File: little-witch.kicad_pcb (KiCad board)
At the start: 4 copper layers, 65 x 30 mm, 56 parts, among them J1 GCT-USB4105, J2 TMJG0803HENL, J3 Conn_ARM_SWD_TagConnect_TC203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, J4 GCT-USB4105, J5 Conn_02x20_Odd_Even, J6 BOOT0_SEL, SW1 SW_Push, U1 CH32V307RCT6, U2 MXL86110C-AQB-R, Y1 SIT8008BI-73-33N-25.000000

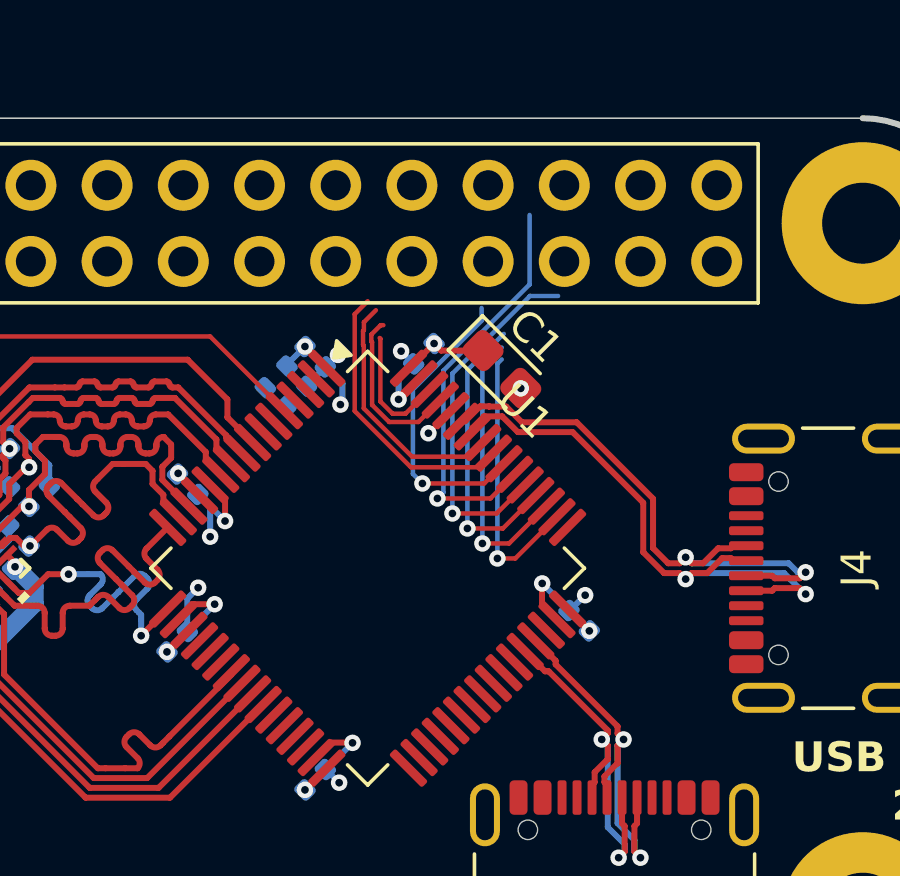
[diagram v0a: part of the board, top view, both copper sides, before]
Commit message: GPIO routing
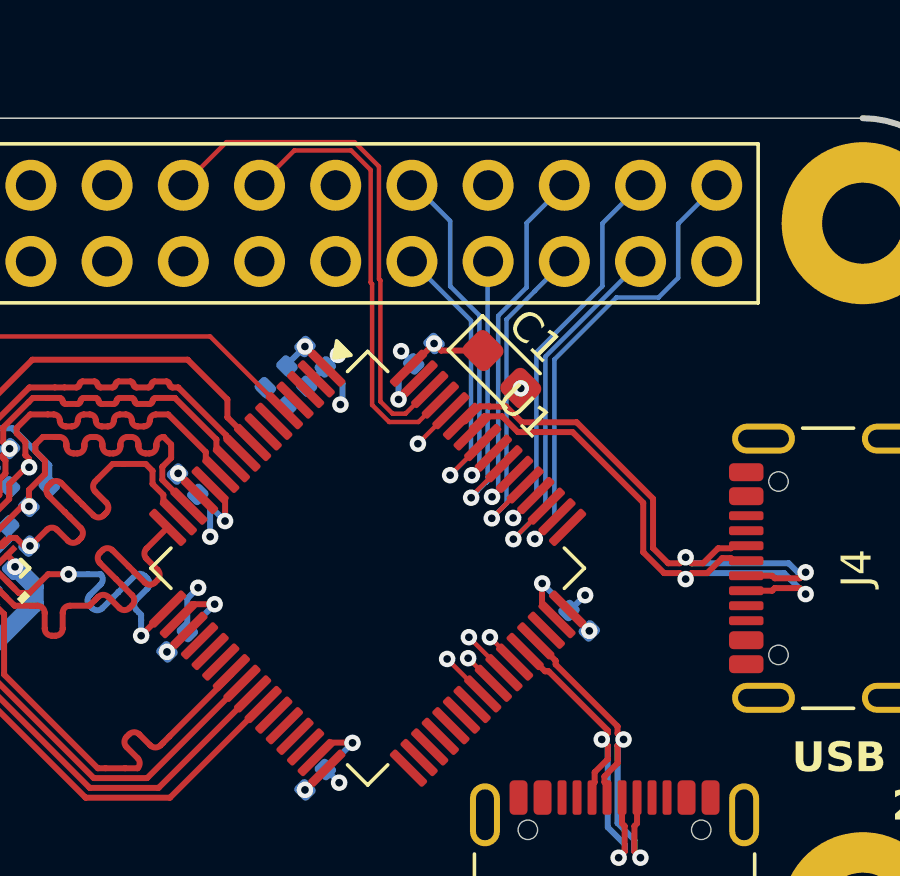
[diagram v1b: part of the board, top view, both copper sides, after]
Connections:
- J5 pad 26: unconnected-(J5-Pin_26-Pad26) -> /PB9
- J5 pad 28: unconnected-(J5-Pin_28-Pad28) -> /PB8
- J5 pad 31: unconnected-(J5-Pin_31-Pad31) -> /PB5
- J5 pad 32: unconnected-(J5-Pin_32-Pad32) -> /PB4
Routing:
- net /PB9: track 4.27 -> 17.5 mm
- net /PB8: track 5.70 -> 15.1 mm
- net /PA15: track 9.25 -> 16.2 mm
- net /PC11: track 9.72 -> 13.9 mm
- net /PC10: track 9.44 -> 12.6 mm
- net /PB4: track 9.43 -> 11.8 mm, vias 0 -> 1
- net /PC9: track 0.00 -> 1.67 mm, vias 0 -> 1
- net /PA9: track 0.00 -> 1.67 mm, vias 0 -> 1
- net /PB5: track 8.29 -> 9.77 mm, vias 0 -> 1
- net /PA8: track 0.00 -> 1.19 mm, vias 0 -> 1
- net /PD2: track 13.6 -> 12.4 mm
- net /PA10: track 0.00 -> 1.17 mm, vias 0 -> 1
- net /PC12: track 12.1 -> 11.1 mm

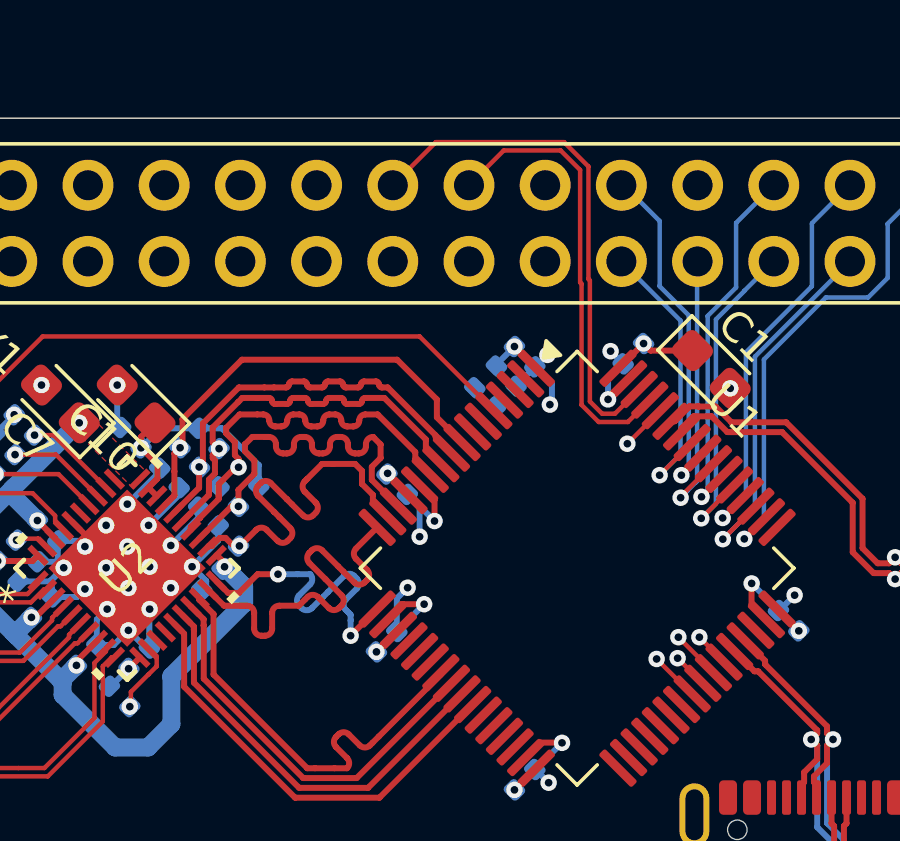
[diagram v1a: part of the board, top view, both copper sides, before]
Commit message: More GPIO routing
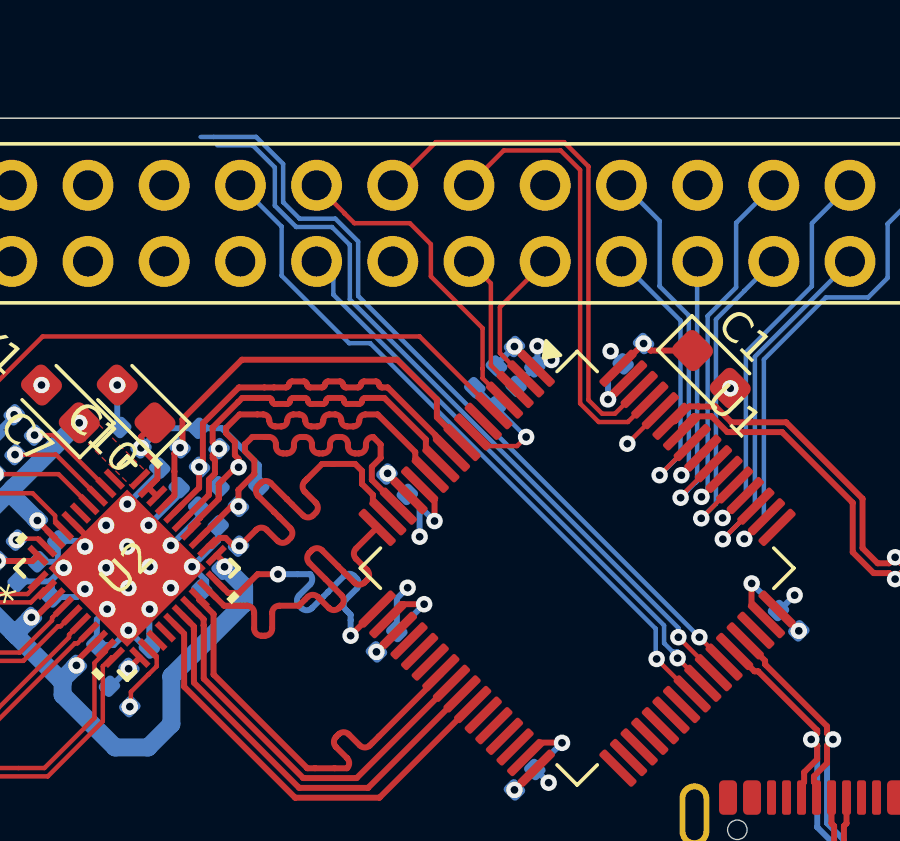
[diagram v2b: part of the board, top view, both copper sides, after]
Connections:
- J5 pad 22: unconnected-(J5-Pin_22-Pad22) -> /PC9
- J5 pad 23: unconnected-(J5-Pin_23-Pad23) -> /PA8
- J5 pad 24: unconnected-(J5-Pin_24-Pad24) -> /PC15
- J5 pad 27: unconnected-(J5-Pin_27-Pad27) -> /PC14
- J5 pad 29: unconnected-(J5-Pin_29-Pad29) -> /PC13
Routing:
- net /PA10: track 1.17 -> 26.5 mm
- net /PA9: track 1.67 -> 25.8 mm
- net /PC9: track 1.67 -> 23.6 mm
- net /PA8: track 1.19 -> 19.5 mm
- net /PC15: track 0.00 -> 10.8 mm
- net /PC13: track 0.00 -> 4.92 mm
- net /PC14: track 0.00 -> 4.90 mm
- net NRST: track 0.00 -> 4.49 mm, vias 0 -> 1
- net GND: track 42.7 -> 42.0 mm

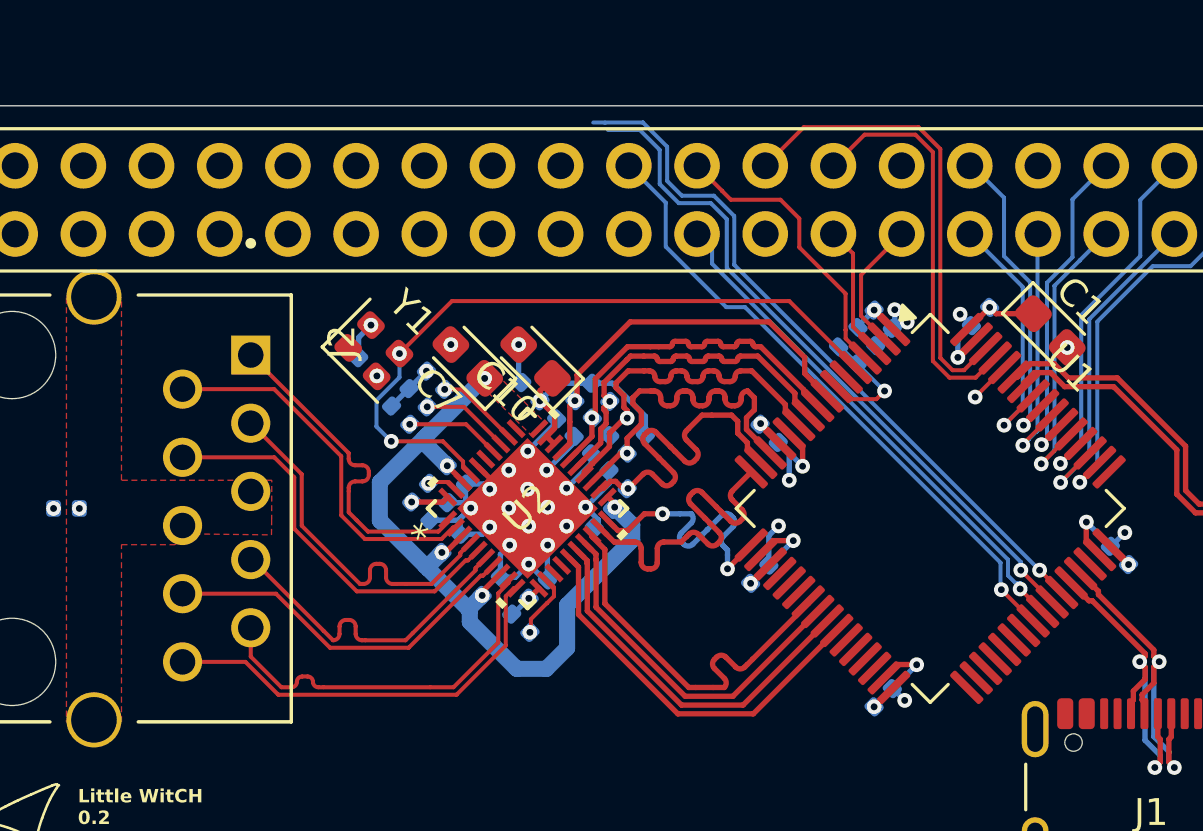
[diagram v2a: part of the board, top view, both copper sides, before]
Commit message: Yet more GPIO routing
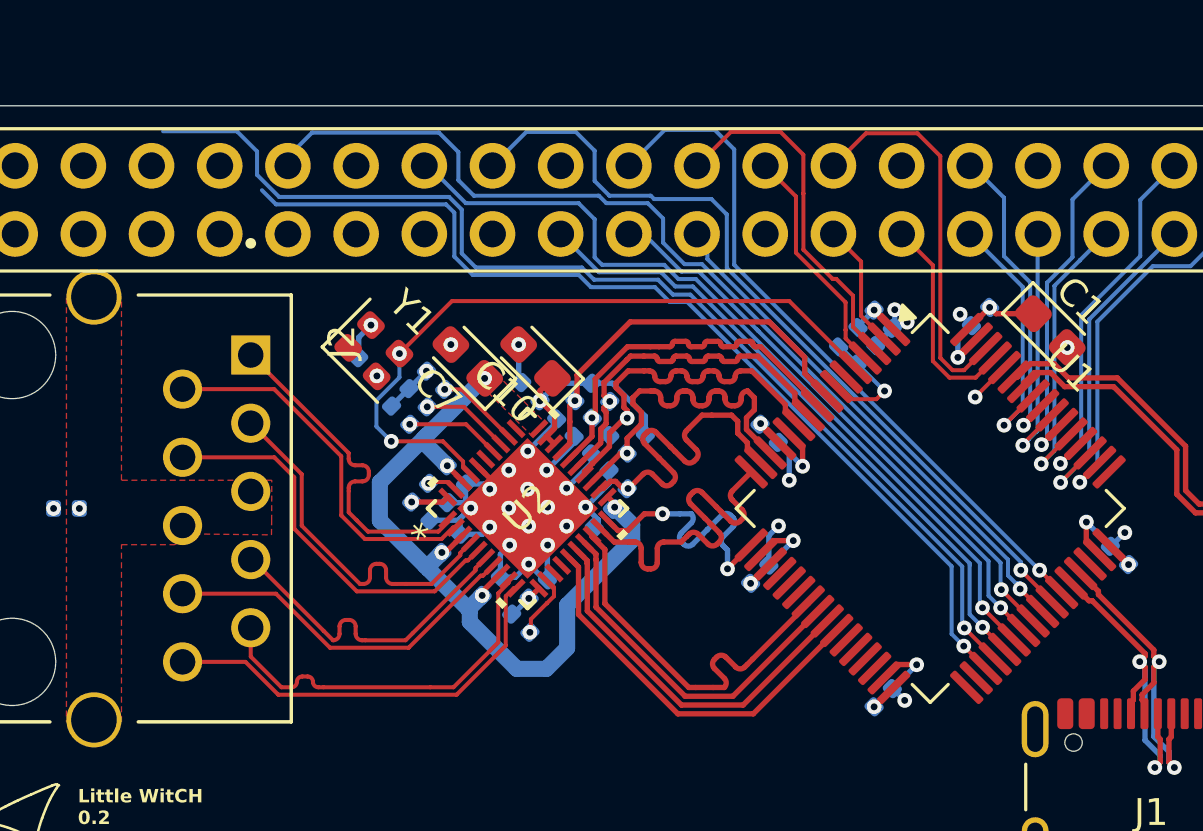
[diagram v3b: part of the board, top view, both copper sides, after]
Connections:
- J5 pad 10: unconnected-(J5-Pin_10-Pad10) -> /PB14
- J5 pad 12: unconnected-(J5-Pin_12-Pad12) -> /PC9
- J5 pad 16: unconnected-(J5-Pin_16-Pad16) -> /PC7
- J5 pad 18: unconnected-(J5-Pin_18-Pad18) -> /PA9
- J5 pad 19: unconnected-(J5-Pin_19-Pad19) -> /PC6
- J5 pad 21: unconnected-(J5-Pin_21-Pad21) -> /PC8
- J5 pad 22: /PC9 -> /PA10
- J5 pad 24: /PC15 -> /PC14
- J5 pad 26: /PB9 -> /PC15
- J5 pad 27: /PC14 -> /PC13
- J5 pad 28: /PB8 -> /PB9
- J5 pad 29: /PC13 -> /PB8
- J5 pad 8: unconnected-(J5-Pin_8-Pad8) -> /PB15
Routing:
- net /PB15: track 0.00 -> 41.9 mm, vias 0 -> 1
- net /PB14: track 0.00 -> 36.8 mm, vias 0 -> 1
- net /PC7: track 0.00 -> 31.1 mm, vias 0 -> 1
- net /PC6: track 0.00 -> 24.1 mm, vias 0 -> 1
- net /PC8: track 0.00 -> 21.7 mm, vias 0 -> 1
- net /PC9: track 23.6 -> 37.7 mm
- net /PC14: track 4.90 -> 13.2 mm
- net /PB8: track 15.1 -> 8.13 mm
- net /PA9: track 25.8 -> 30.6 mm
- net /PB9: track 17.5 -> 14.6 mm
- net /PC15: track 10.8 -> 8.70 mm

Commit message: GPIO fully routed
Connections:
- J5 pad 11: unconnected-(J5-Pin_11-Pad11) -> /PB1
- J5 pad 13: unconnected-(J5-Pin_13-Pad13) -> /PB10
- J5 pad 15: unconnected-(J5-Pin_15-Pad15) -> /PB11
- J5 pad 3: unconnected-(J5-Pin_3-Pad3) -> /PA6
- J5 pad 5: unconnected-(J5-Pin_5-Pad5) -> /PA5
- J5 pad 7: unconnected-(J5-Pin_7-Pad7) -> /PA4
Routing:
- net /PA6: track 0.00 -> 39.3 mm, vias 0 -> 1
- net /PA5: track 0.00 -> 36.2 mm, vias 0 -> 1
- net /PA4: track 0.00 -> 31.5 mm, vias 0 -> 1
- net /PB10: track 0.00 -> 30.6 mm, vias 0 -> 1
- net /PB1: track 0.00 -> 30.2 mm, vias 0 -> 1
- net /PB11: track 0.00 -> 28.9 mm, vias 0 -> 1
- net /PB14: track 36.8 -> 38.7 mm
- net /PB2: track 0.00 -> 1.18 mm, vias 0 -> 1
- net /PB15: track 41.9 -> 43.1 mm

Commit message: Ethernet LEDs and start of power
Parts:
- R3, R4: moved to B.Cu
- moved R3 25.0 mm to (151.4, 125.7), turned to 180 degrees
- moved R4 21.3 mm to (155.6, 125.7), turned to 180 degrees
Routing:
- net USB1_VBUS: track 0.00 -> 36.7 mm
- net ETH_LED2: track 3.32 -> 32.0 mm, vias 1 -> 2
- net ETH_LED1: track 3.10 -> 29.9 mm, vias 1 -> 2
- net Net-(J2-Pad12): track 0.00 -> 1.79 mm
- net Net-(J2-Pad14): track 0.00 -> 1.77 mm
